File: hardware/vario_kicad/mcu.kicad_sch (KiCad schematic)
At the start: 17 parts, among them P2 USB_C_Plug_USB2.0, U5 STM32L072CBTx, Y1 Crystal

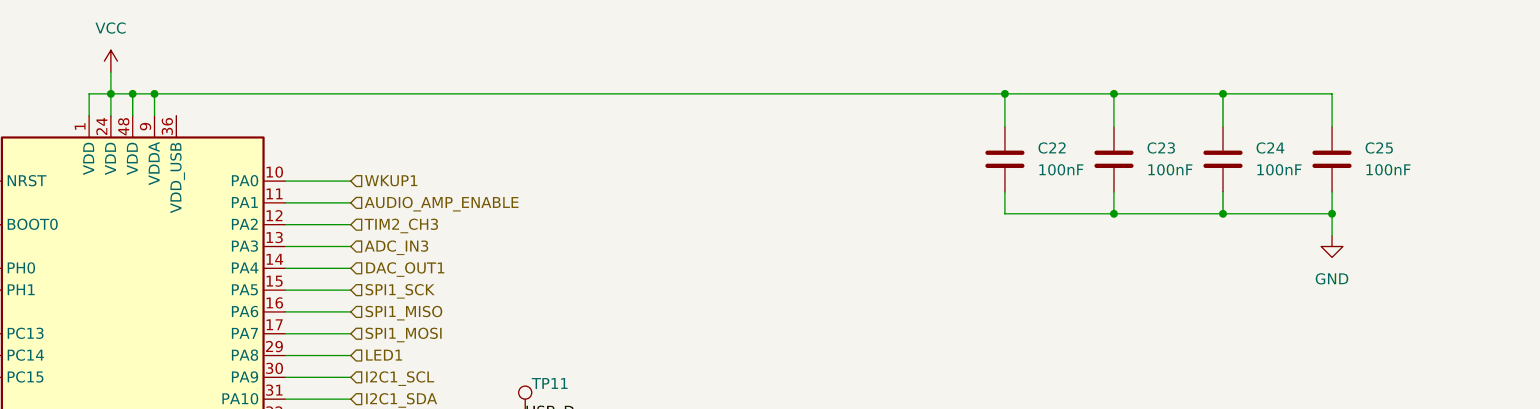
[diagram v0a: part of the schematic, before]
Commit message: add hw design guide
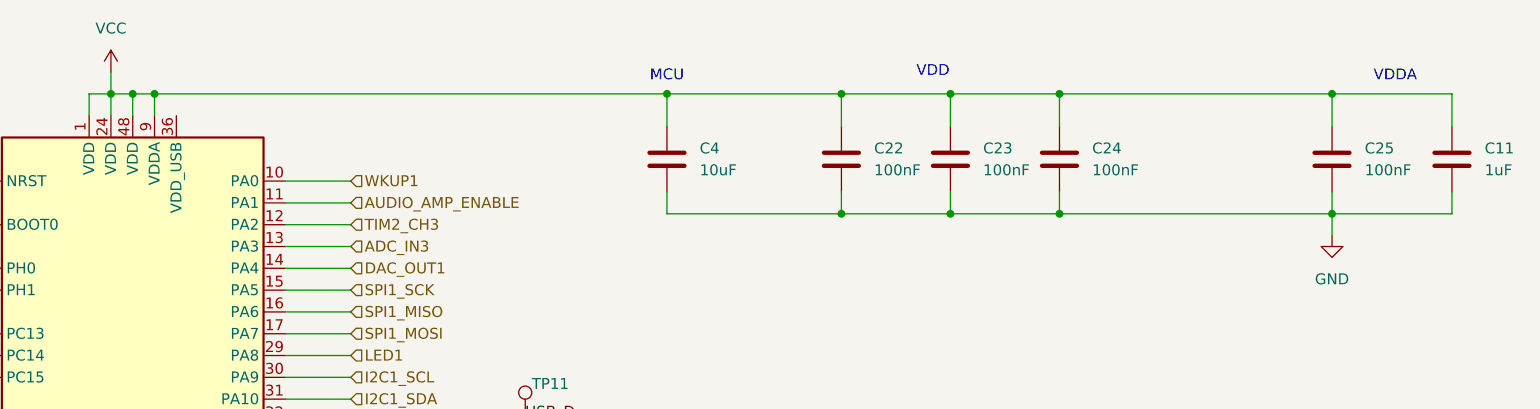
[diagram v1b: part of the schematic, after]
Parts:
- added C11: 1uF, symbol Device:C
- added C4: 10uF, symbol Device:C
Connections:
- net GND: now also C11.2, C4.2
- net VCC: now also C11.1, C4.1
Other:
- note added: "MCU"
- note added: "VDD"
- note added: "VDDA"
- moved on the sheet: C22, C23, C24

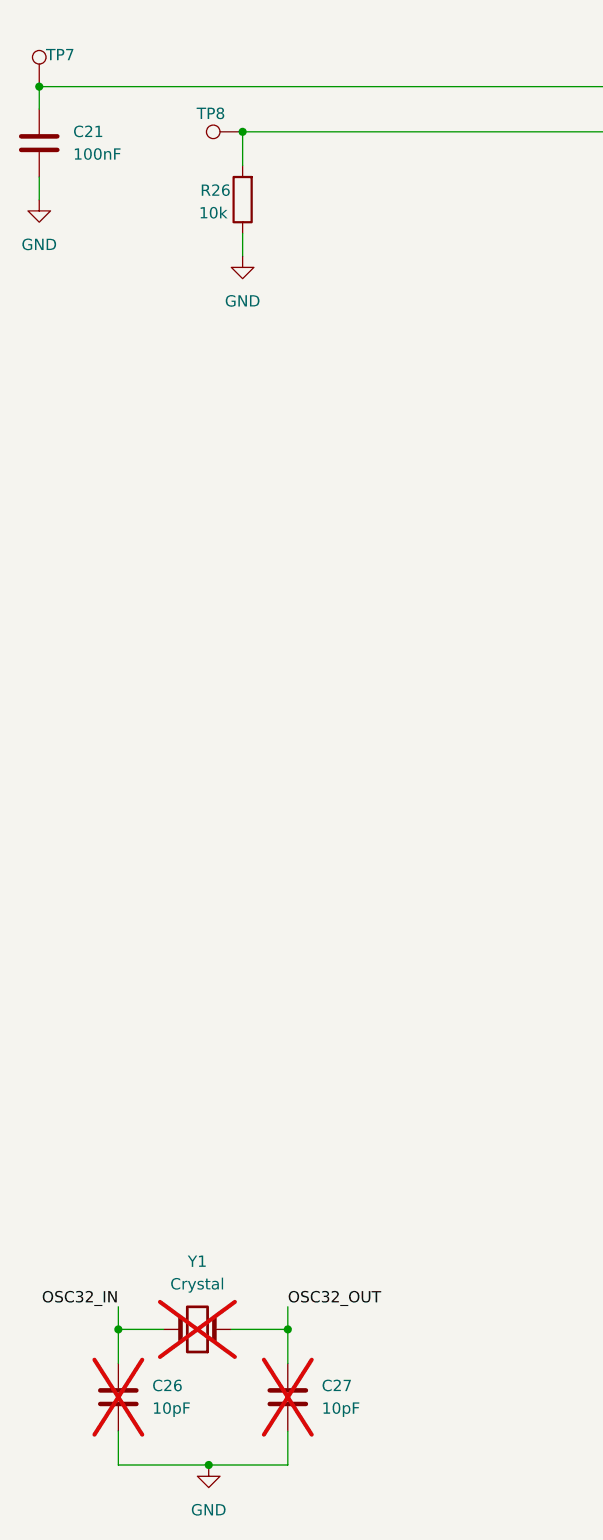
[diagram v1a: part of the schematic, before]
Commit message: update footprints, add LSE oscillator
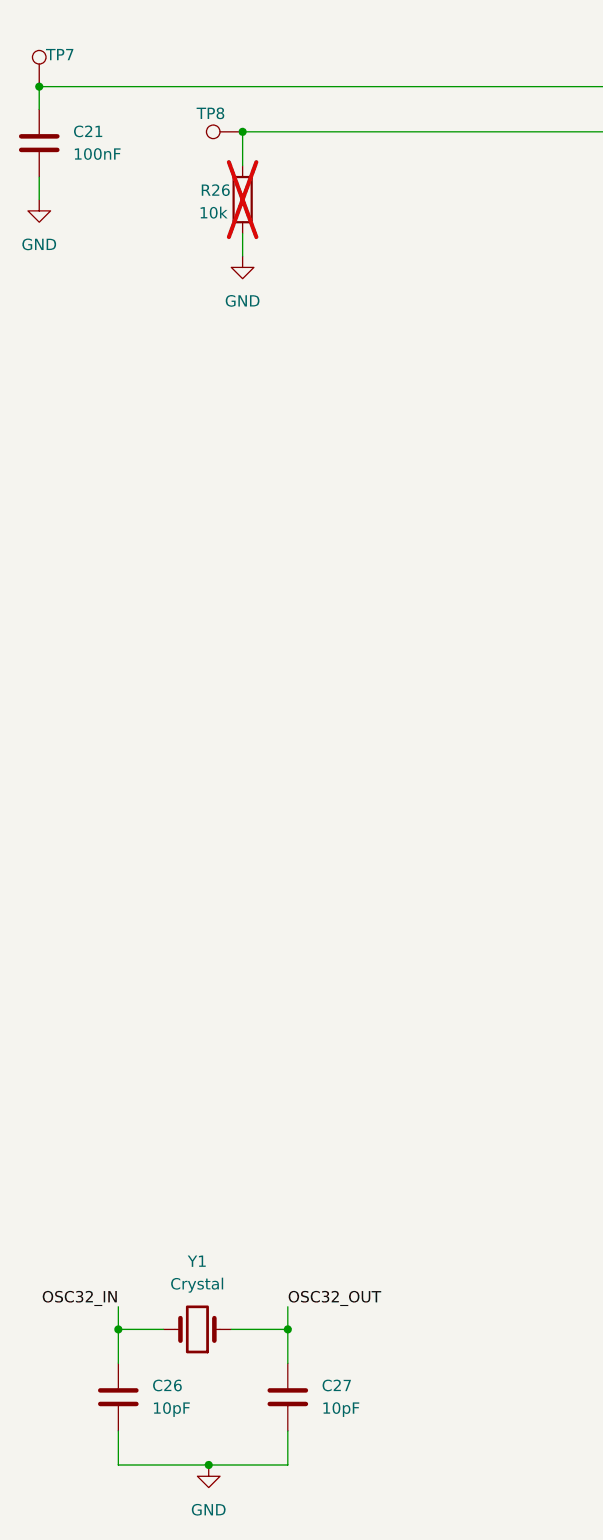
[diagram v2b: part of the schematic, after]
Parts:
- C11, C22, C23, C24, C25, C4: footprint (none) -> Capacitor_SMD:C_0603_1608Metric
- C26, C27: footprint (none) -> Capacitor_SMD:C_0402_1005Metric; now fitted
- R26: footprint (none) -> Resistor_SMD:R_0402_1005Metric; now not fitted
- R27: footprint (none) -> Resistor_SMD:R_0402_1005Metric
- TP11, TP12, TP7, TP8: footprint (none) -> TestPoint:TestPoint_Pad_D1.0mm
- Y1: footprint Crystal:Crystal_SMD_3215-2Pin_3.2x1.5mm -> Crystal:Crystal_SMD_2012-2Pin_2.0x1.2mm_HandSoldering; now fitted
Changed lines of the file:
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@@
 			)
 		)
-		(property "Footprint" ""
+		(property "Footprint" "Capacitor_SMD:C_0603_1608Metric"
 			(at 298.1452 105.41 0)
 			(effects
@@
 			)
 		)
-		(property "Footprint" ""
+		(property "Footprint" "Capacitor_SMD:C_0603_1608Metric"
 			(at 266.3952 105.41 0)
 			(effects
@@
 			)
 		)
-		(property "Footprint" ""
+		(property "Footprint" "Capacitor_SMD:C_0603_1608Metric"
 			(at 220.6752 105.41 0)
 			(effects
@@
 			)
 		)
-		(property "Footprint" ""
+		(property "Footprint" "TestPoint:TestPoint_Pad_D1.0mm"
 			(at 198.12 134.62 0)
 			(effects
@@
 			)
 		)
-		(property "Footprint" ""
+		(property "Footprint" "Capacitor_SMD:C_0603_1608Metric"
 			(at 253.6952 105.41 0)
 			(effects
@@
 			)
 		)
-		(property "Footprint" ""
+		(property "Footprint" "TestPoint:TestPoint_Pad_D1.0mm"
 			(at 208.28 132.08 0)
 			(effects
@@
 			)
 		)
-		(property "Footprint" ""
+		(property "Footprint" "Capacitor_SMD:C_0603_1608Metric"
 			(at 240.9952 105.41 0)
 			(effects
@@
 		(in_bom yes)
 		(on_board yes)
-		(dnp no)
+		(dnp yes)
 		(property "Reference" "R26"
 			(at 49.022 115.824 0)
@@
 			)
 		)
-		(property "Footprint" ""
+		(property "Footprint" "Resistor_SMD:R_0402_1005Metric"
 			(at 53.848 116.84 90)
 			(effects
@@
 			)
 		)
-		(property "Footprint" ""
+		(property "Footprint" "Capacitor_SMD:C_0603_1608Metric"
 			(at 312.1152 105.41 0)
 			(effects
@@
 			)
 		)
-		(property "Footprint" ""
+		(property "Footprint" "TestPoint:TestPoint_Pad_D1.0mm"
 			(at 52.07 104.14 0)
 			(effects
@@
 		(in_bom yes)
 		(on_board yes)
-		(dnp yes)
+		(dnp no)
 		(fields_autoplaced yes)
 		(property "Reference" "C26"
@@
 			)
 		)
-		(property "Footprint" ""
+		(property "Footprint" "Capacitor_SMD:C_0402_1005Metric"
 			(at 39.0652 255.27 0)
 			(effects
@@
 		(in_bom yes)
 		(on_board yes)
-		(dnp yes)
+		(dnp no)
 		(fields_autoplaced yes)
 		(property "Reference" "C27"
@@
 			)
 		)
-		(property "Footprint" ""
+		(property "Footprint" "Capacitor_SMD:C_0402_1005Metric"
 			(at 58.1152 255.27 0)
 			(effects
@@
 			)
 		)
-		(property "Footprint" ""
+		(property "Footprint" "Resistor_SMD:R_0402_1005Metric"
 			(at 270.51 173.228 90)
 			(effects
@@
 			)
 		)
-		(property "Footprint" ""
+		(property "Footprint" "TestPoint:TestPoint_Pad_D1.0mm"
 			(at 34.29 104.14 0)
 			(effects
@@
 		(in_bom yes)
 		(on_board yes)
-		(dnp yes)
+		(dnp no)
 		(fields_autoplaced yes)
 		(property "Reference" "Y1"
@@
 			)
 		)
-		(property "Footprint" "Crystal:Crystal_SMD_3215-2Pin_3.2x1.5mm"
+		(property "Footprint" "Crystal:Crystal_SMD_2012-2Pin_2.0x1.2mm_HandSoldering"
 			(at 46.99 243.84 0)
 			(effects
@@
 			)
 		)
-		(property "Datasheet" ""
+		(property "Datasheet" "https://www.lcsc.com/product-detail/Crystals_Seiko-Epson-X1A0000610006_C99009.html"
 			(at 46.99 243.84 0)
 			(effects

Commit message: start layout
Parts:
- removed P2: USB_C_Plug_USB2.0, symbol_lib:my_usbc, symbol Connector:USB_C_Plug_USB2.0
- removed R27: 5k1, Resistor_SMD:R_0402_1005Metric, symbol Device:R
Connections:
- net VCC: now also U5.36 (VDD_USB)
- no-connect marks 12 -> 11

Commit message: v1 review of mcu
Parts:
- removed TP7, TP8: ~, TestPoint:TestPoint_Pad_D1.0mm, symbol Connector:TestPoint
- added C12: 100nF, Capacitor_SMD:C_0603_1608Metric, symbol Device:C
- R26: now fitted
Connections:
- net BOOT0: now also J2.5 (BOOT0), C12.1
- net GND: now also J2.6 (GND), C12.2; no longer J2.4 (GND)
- net NRST: now also J2.4 (NRST)
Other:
- moved on the sheet: C21, C26, C27, Y1

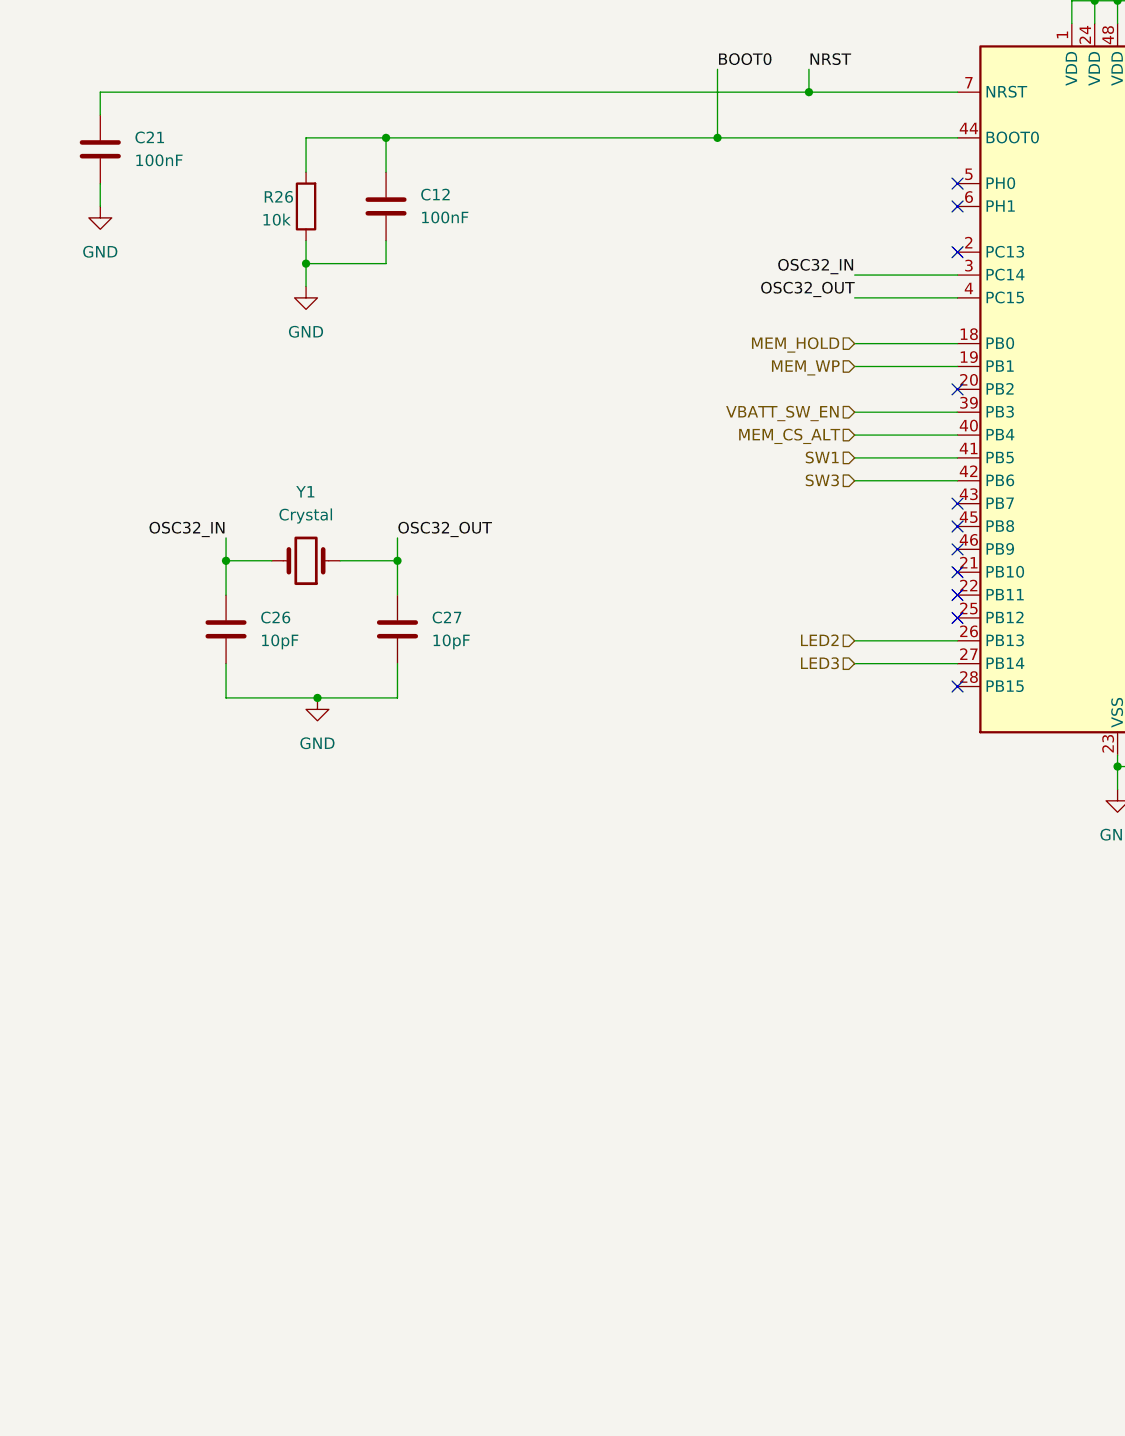
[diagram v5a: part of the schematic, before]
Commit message: add HSE to the MCU
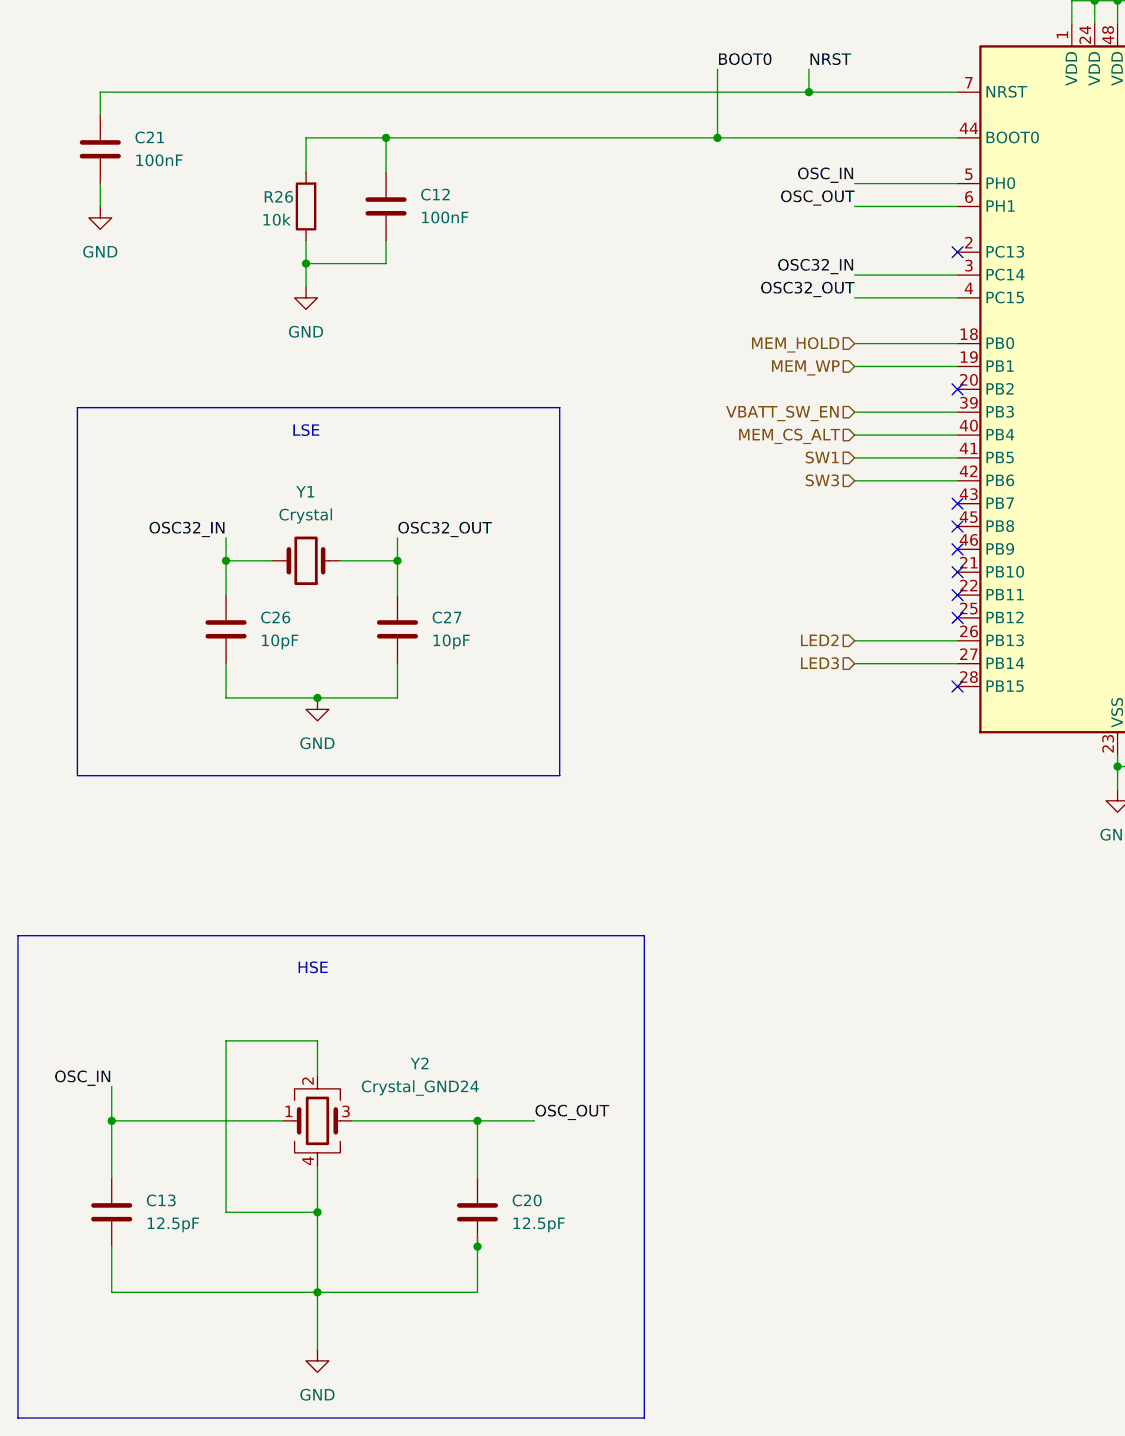
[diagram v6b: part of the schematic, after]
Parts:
- added C13, C20: 12.5pF, symbol Device:C
- added Y2: Crystal_GND24, Crystal:Crystal_SMD_3225-4Pin_3.2x2.5mm_HandSoldering, symbol Device:Crystal_GND24
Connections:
- net GND: now also C13.2, C20.2, Y2.2, Y2.4
- net OSC_IN: now reaches U5.5 (PH0)
- net OSC_IN: now also C13.1, Y2.1
- net OSC_OUT: now reaches U5.6 (PH1)
- net OSC_OUT: now also C20.1, Y2.3
- no-connect marks 11 -> 9
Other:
- note added: "HSE"
- note added: "LSE"

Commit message: add footprints
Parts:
- C13, C20: footprint (none) -> Capacitor_SMD:C_0402_1005Metric
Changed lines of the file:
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@@
 			)
 		)
-		(property "Footprint" ""
+		(property "Footprint" "Capacitor_SMD:C_0402_1005Metric"
 			(at 46.6852 232.41 0)
 			(effects
@@
 			)
 		)
-		(property "Footprint" ""
+		(property "Footprint" "Capacitor_SMD:C_0402_1005Metric"
 			(at 87.3252 232.41 0)
 			(effects

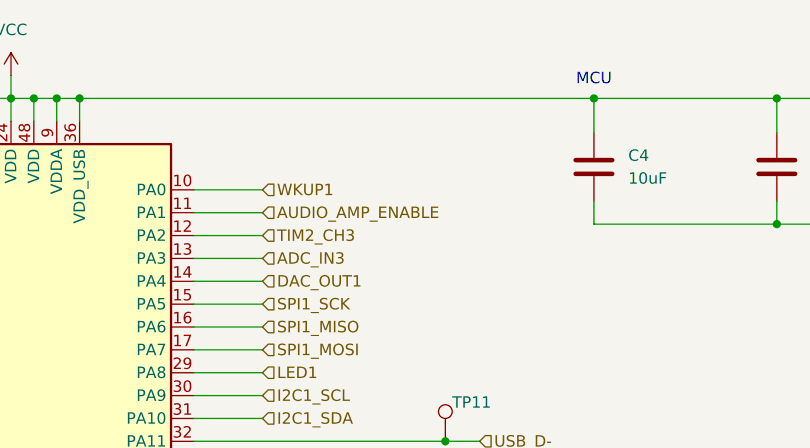
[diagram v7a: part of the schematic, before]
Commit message: fix memory schematic, update button switches
- fix miso/mosi mistake: miso->miso, mosi->mosi
- WKUP1 needs a rising edge to wake up the MCU, so all switch logic was
  reversed
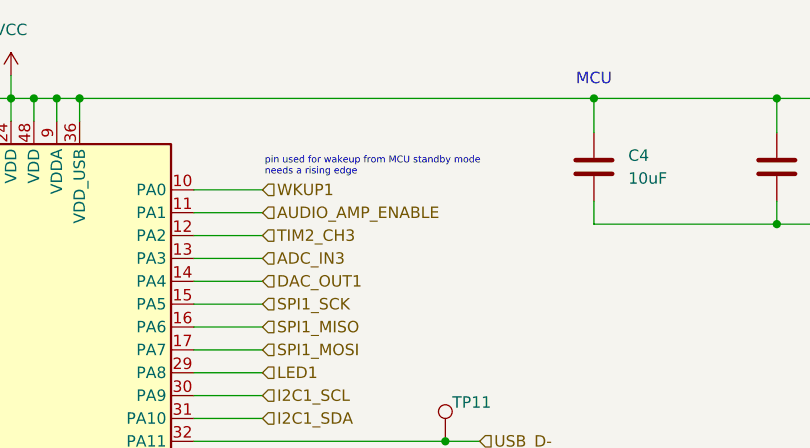
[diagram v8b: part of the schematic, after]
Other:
- note added: "pin used for wakeup from MCU standby mode needs a rising edge"
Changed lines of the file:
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@@
+		)
+	)
+	(text "pin used for wakeup from MCU standby mode\nneeds a rising edge"
+		(exclude_from_sim no)
+		(at 183.134 101.6 0)
+		(effects
+			(font
+				(size 0.762 0.762)
+			)
+			(justify left)
 		)
 	)
